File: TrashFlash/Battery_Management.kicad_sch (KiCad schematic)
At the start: 13 parts, among them IC10 BQ24230RGTR, IC3 BQ27426YZFR, IC9 BQ29732DSER, Q5 PMDPB30XNAX

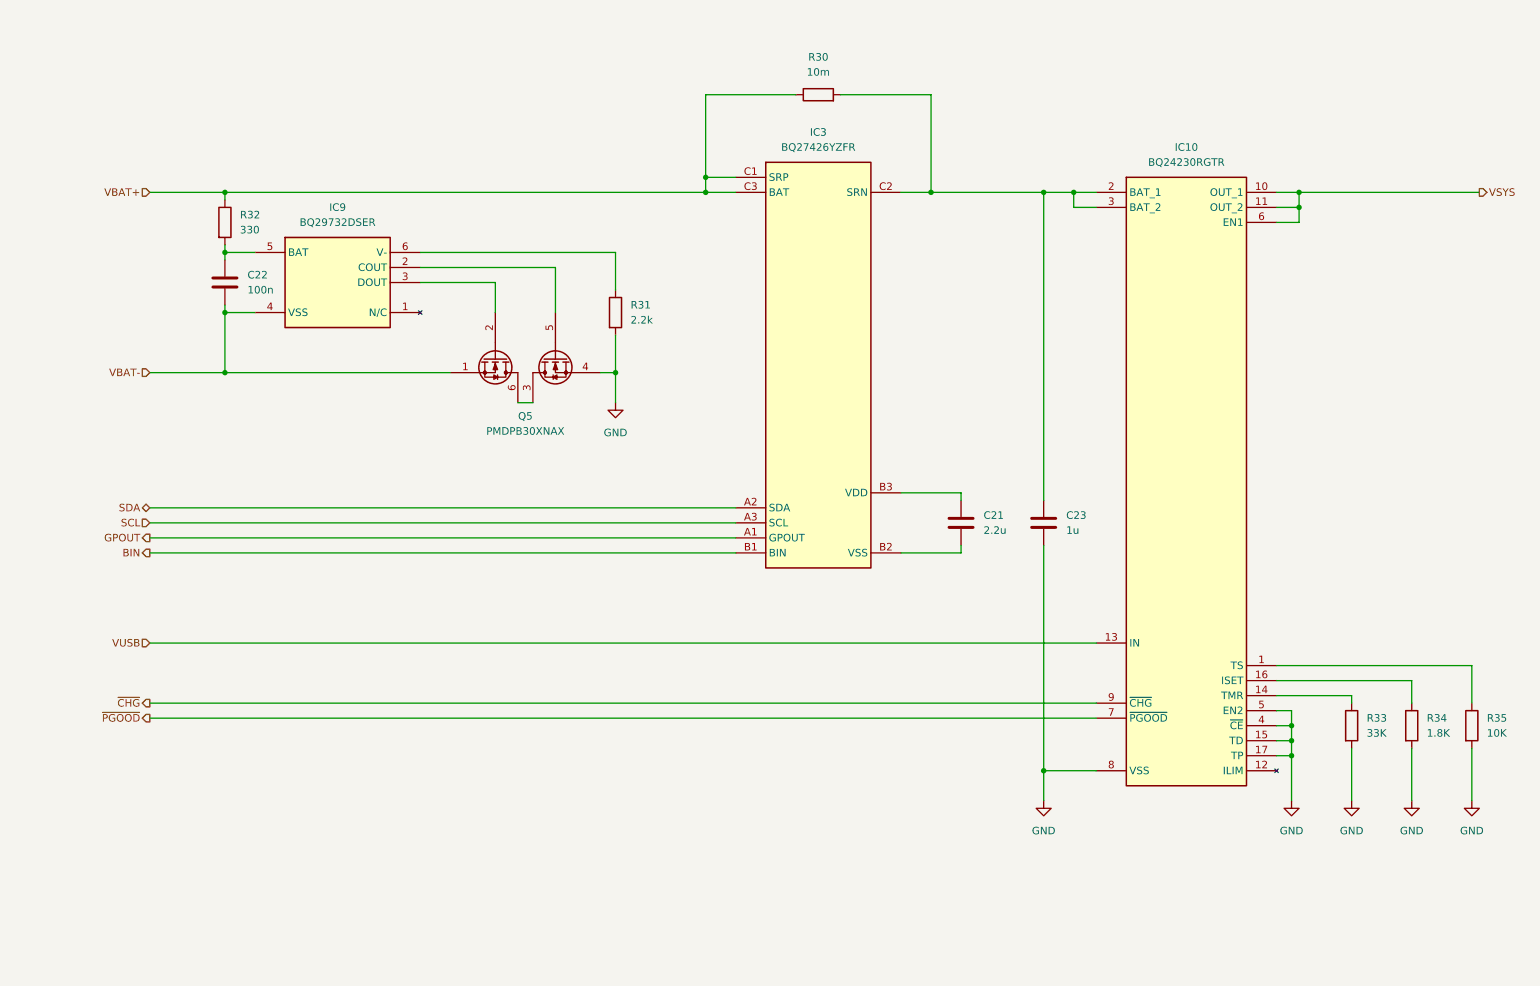
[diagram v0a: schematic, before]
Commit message: Added USB and powernets
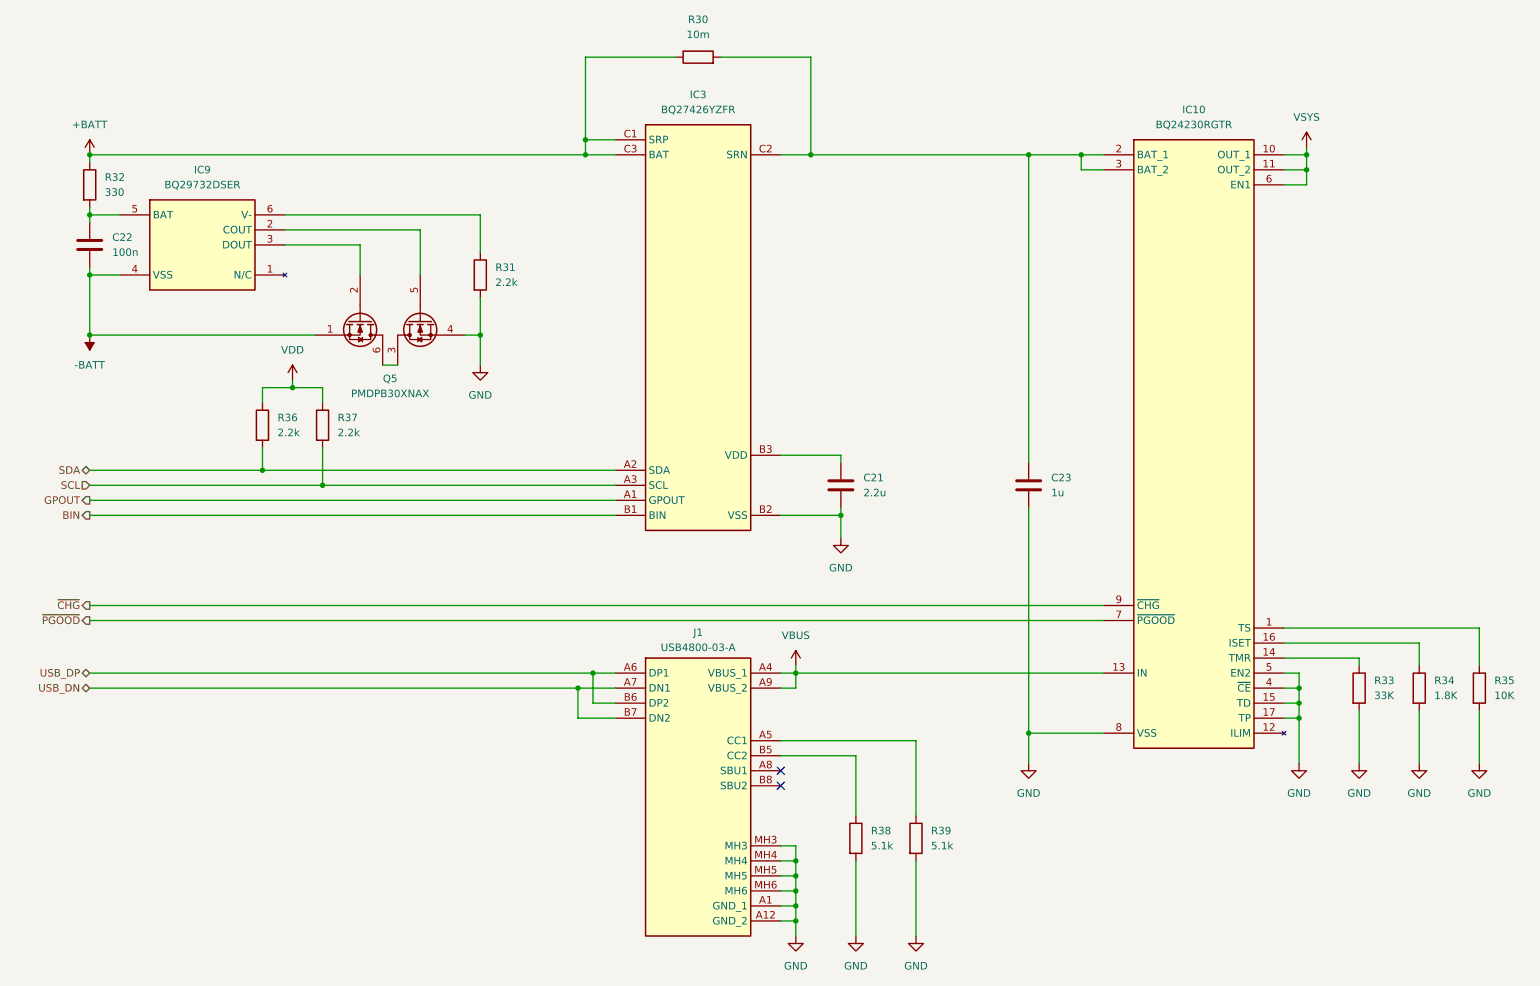
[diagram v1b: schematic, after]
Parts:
- added J1: USB4800-03-A, USB480003A, symbol TrashFlash:USB4800-03-A
- added R36, R37: 2.2k, symbol Device:R
- added R38, R39: 5.1k, symbol Device:R
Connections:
- net GND: now also C21.2, IC3.B2 (VSS), J1.A1 (GND_1), J1.A12 (GND_2), J1.MH3, J1.MH4, J1.MH5, J1.MH6, R38.2, R39.2
- net SCL: now also R37.2
- net SDA: now also R36.2
- net VBAT+ renamed +BATT
- net VBAT- renamed -BATT
- net VUSB renamed VBUS
- net VBUS: now also J1.A4 (VBUS_1), J1.A9 (VBUS_2)
- new net: J1.A5 (CC1), R39.1
- new net: J1.B5 (CC2), R38.1
- new net USB_DN: J1.A7 (DN1), J1.B7 (DN2)
- new net USB_DP: J1.A6 (DP1), J1.B6 (DP2)
- new net VDD: R36.1, R37.1
- no-connect marks 0 -> 2
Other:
- moved on the sheet: C21, C22, C23, IC10, IC3, IC9, Q5, R30, R31, R32, R33, R34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

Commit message: Rotary encoder added + 3D stuff
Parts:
- C21, C23: footprint (none) -> Capacitor_SMD:C_0603_1608Metric
- C22: footprint (none) -> Capacitor_SMD:C_0402_1005Metric
- IC10: footprint QFN50P300X300X100-17N-D -> TrashFlash:QFN50P300X300X100-17N-D
- IC3: footprint BGA9C50P3X3_158X162X62 -> TrashFlash:BGA9C50P3X3_158X162X62
- IC9: footprint SON50P150X150X80-6N -> TrashFlash:SON50P150X150X80-6N
- J1: footprint USB480003A -> TrashFlash:USB480003A
- Q5: footprint PMDPB30XNAX -> TrashFlash:PMDPB30XNAX
- R30: footprint (none) -> Resistor_SMD:R_0603_1608Metric
- R31, R32, R33, R34, R35, R36, R37, R38, R39: footprint (none) -> Resistor_SMD:R_0402_1005Metric
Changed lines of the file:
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@@
 			)
 		)
-		(property "Footprint" ""
+		(property "Footprint" "Capacitor_SMD:C_0603_1608Metric"
 			(at 191.4652 97.79 0)
 			(effects
@@
 			)
 		)
-		(property "Footprint" "SON50P150X150X80-6N"
+		(property "Footprint" "TrashFlash:SON50P150X150X80-6N"
 			(at 74.93 149.53 0)
 			(effects
@@
 			)
 		)
-		(property "Footprint" "BGA9C50P3X3_158X162X62"
+		(property "Footprint" "TrashFlash:BGA9C50P3X3_158X162X62"
 			(at 158.75 135.56 0)
 			(effects
@@
 			)
 		)
-		(property "Footprint" ""
+		(property "Footprint" "Capacitor_SMD:C_0402_1005Metric"
 			(at 32.7152 57.15 0)
 			(effects
@@
 			)
 		)
-		(property "Footprint" "USB480003A"
+		(property "Footprint" "TrashFlash:USB480003A"
 			(at 135.128 198.374 0)
 			(effects
@@
 			)
 		)
-		(property "Footprint" ""
+		(property "Footprint" "Capacitor_SMD:C_0603_1608Metric"
 			(at 159.7152 97.79 0)
 			(effects
@@
 			)
 		)
-		(property "Footprint" "PMDPB30XNAX"
+		(property "Footprint" "TrashFlash:PMDPB30XNAX"
 			(at 109.22 163.5 0)
 			(effects
@@
 			)
 		)
-		(property "Footprint" "QFN50P300X300X100-17N-D"
+		(property "Footprint" "TrashFlash:QFN50P300X300X100-17N-D"
 			(at 207.264 85.344 0)
 			(effects
@@
 			)
 		)
-		(property "Footprint" ""
+		(property "Footprint" "Resistor_SMD:R_0402_1005Metric"
 			(at 96.012 58.42 90)
 			(effects
@@
 			)
 		)
-		(property "Footprint" ""
+		(property "Footprint" "Resistor_SMD:R_0402_1005Metric"
 			(at 169.672 153.67 90)
 			(effects
@@
 			)
 		)
-		(property "Footprint" ""
+		(property "Footprint" "Resistor_SMD:R_0402_1005Metric"
 			(at 264.922 128.27 90)
 			(effects
@@
 			)
 		)
-		(property "Footprint" ""
+		(property "Footprint" "Resistor_SMD:R_0402_1005Metric"
 			(at 254.762 128.27 90)
 			(effects
@@
 			)
 		)
-		(property "Footprint" ""
+		(property "Footprint" "Resistor_SMD:R_0603_1608Metric"
 			(at 134.62 23.368 90)
 			(effects
@@
 			)
 		)
-		(property "Footprint" ""
+		(property "Footprint" "Resistor_SMD:R_0402_1005Metric"
 			(at 59.182 83.82 90)
 			(effects
@@
 			)
 		)
-		(property "Footprint" ""
+		(property "Footprint" "Resistor_SMD:R_0402_1005Metric"
 			(at 159.512 153.67 90)
 			(effects
@@
 			)
 		)
-		(property "Footprint" ""
+		(property "Footprint" "Resistor_SMD:R_0402_1005Metric"
 			(at 244.602 128.27 90)
 			(effects
@@
 			)
 		)
-		(property "Footprint" ""
+		(property "Footprint" "Resistor_SMD:R_0402_1005Metric"
 			(at 69.342 83.82 90)
 			(effects
@@
 			)
 		)
-		(property "Footprint" ""
+		(property "Footprint" "Resistor_SMD:R_0402_1005Metric"
 			(at 29.972 43.18 90)
 			(effects

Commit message: Footprints 3D model fixed
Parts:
- IC10: footprint TrashFlash:QFN50P300X300X100-17N-D -> QFN50P300X300X100-17N-D
- IC3: footprint TrashFlash:BGA9C50P3X3_158X162X62 -> BGA9C50P3X3_158X162X62
- IC9: footprint TrashFlash:SON50P150X150X80-6N -> SON50P150X150X80-6N
- J1: footprint TrashFlash:USB480003A -> USB480003A
- Q5: footprint TrashFlash:PMDPB30XNAX -> PMDPB30XNAX
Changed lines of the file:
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@@
 			)
 		)
-		(property "Footprint" "TrashFlash:SON50P150X150X80-6N"
+		(property "Footprint" "SON50P150X150X80-6N"
 			(at 74.93 149.53 0)
 			(effects
@@
 			)
 		)
-		(property "Footprint" "TrashFlash:BGA9C50P3X3_158X162X62"
+		(property "Footprint" "BGA9C50P3X3_158X162X62"
 			(at 158.75 135.56 0)
 			(effects
@@
 			)
 		)
-		(property "Footprint" "TrashFlash:USB480003A"
+		(property "Footprint" "USB480003A"
 			(at 135.128 198.374 0)
 			(effects
@@
 			)
 		)
-		(property "Footprint" "TrashFlash:PMDPB30XNAX"
+		(property "Footprint" "PMDPB30XNAX"
 			(at 109.22 163.5 0)
 			(effects
@@
 			)
 		)
-		(property "Footprint" "TrashFlash:QFN50P300X300X100-17N-D"
+		(property "Footprint" "QFN50P300X300X100-17N-D"
 			(at 207.264 85.344 0)
 			(effects

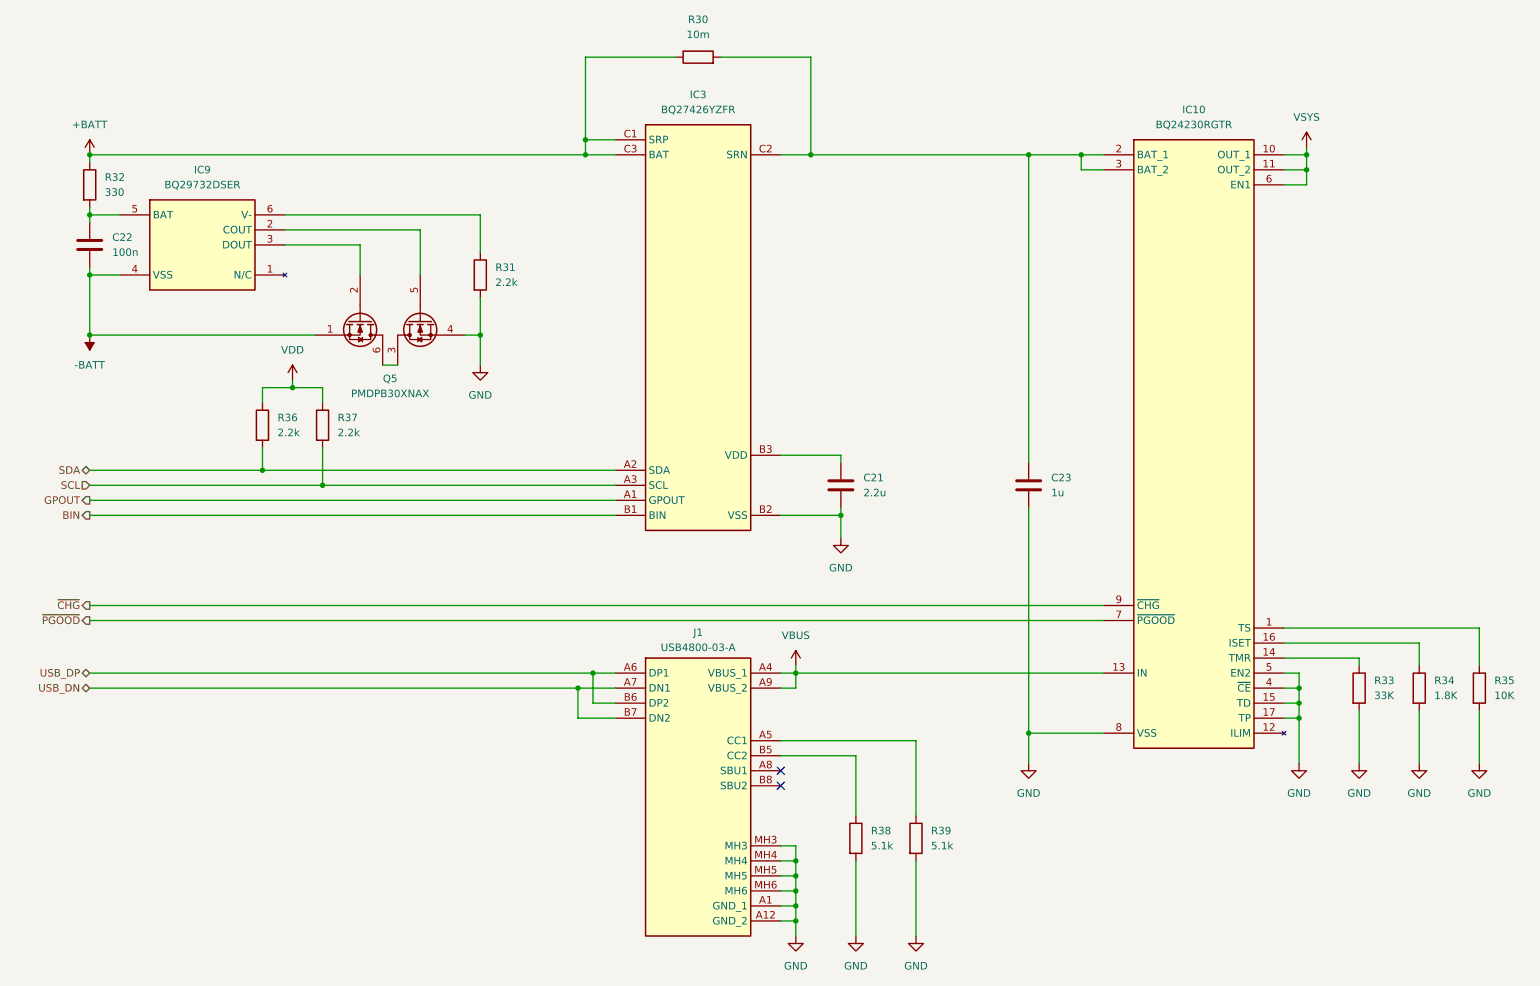
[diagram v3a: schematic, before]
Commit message: Added netlabels / cleaned up schematic
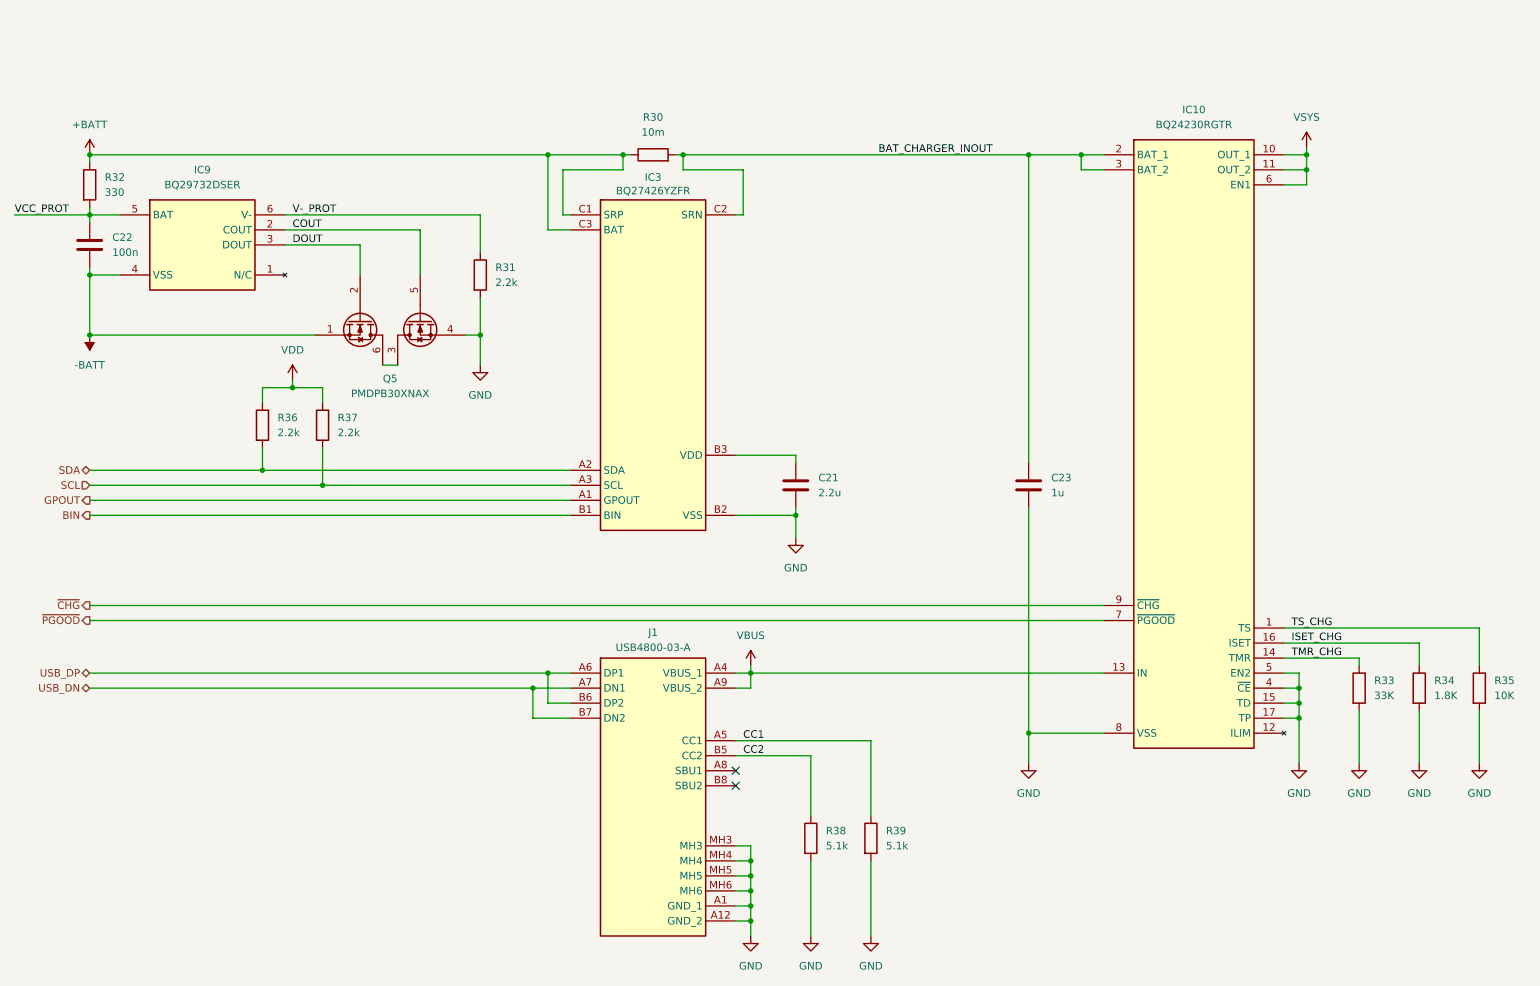
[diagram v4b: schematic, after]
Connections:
- net BAT_CHARGER_INOUT: now reaches C23.1, IC10.2 (BAT_1), IC10.3 (BAT_2), IC3.C2 (SRN), R30.2
- net COUT: now reaches IC9.2 (COUT), Q5.5
- net DOUT: now reaches IC9.3 (DOUT), Q5.2
- net VCC_PROT: now reaches C22.1, IC9.5 (BAT), R32.2
- net V-_PROT: now reaches IC9.6 (V-), R31.1
- net CC1: now reaches J1.A5 (CC1), R39.1
- net CC2: now reaches J1.B5 (CC2), R38.1
- net TS_CHG: now reaches IC10.1 (TS), R35.1
- net TMR_CHG: now reaches IC10.14 (TMR), R33.1
- net ISET_CHG: now reaches IC10.16 (ISET), R34.1
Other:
- moved on the sheet: C21, IC3, J1, R30, R38, R39

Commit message: Added 3D-models to footprints, PCB outline and component placement
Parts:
- IC10: footprint QFN50P300X300X100-17N-D -> TrashFlash:QFN50P300X300X100-17N-D
- IC3: footprint BGA9C50P3X3_158X162X62 -> TrashFlash:BGA9C50P3X3_158X162X62
- IC9: footprint SON50P150X150X80-6N -> TrashFlash:SON50P150X150X80-6N
- J1: footprint USB480003A -> TrashFlash:USB480003A
- Q5: footprint PMDPB30XNAX -> TrashFlash:PMDPB30XNAX
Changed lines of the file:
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@@
 			)
 		)
-		(property "Footprint" "SON50P150X150X80-6N"
+		(property "Footprint" "TrashFlash:SON50P150X150X80-6N"
 			(at 74.93 149.53 0)
 			(effects
@@
 			)
 		)
-		(property "Footprint" "BGA9C50P3X3_158X162X62"
+		(property "Footprint" "TrashFlash:BGA9C50P3X3_158X162X62"
 			(at 142.24 140.64 0)
 			(effects
@@
 			)
 		)
-		(property "Footprint" "USB480003A"
+		(property "Footprint" "TrashFlash:USB480003A"
 			(at 127.508 198.374 0)
 			(effects
@@
 			)
 		)
-		(property "Footprint" "PMDPB30XNAX"
+		(property "Footprint" "TrashFlash:PMDPB30XNAX"
 			(at 109.22 163.5 0)
 			(effects
@@
 			)
 		)
-		(property "Footprint" "QFN50P300X300X100-17N-D"
+		(property "Footprint" "TrashFlash:QFN50P300X300X100-17N-D"
 			(at 207.264 85.344 0)
 			(effects
